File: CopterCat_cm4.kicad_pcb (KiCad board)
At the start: 4 copper layers, 99 parts, among them IC1 LY68L6400SLIT, J1 Micro_SD_Card, J2 Conn_01x08_Male, J3 Conn_01x08_Male, J4 Conn_01x08_Male, J5 XT30, U1 STM32H753IIKx, U10 ESP32-S2FH4, U11 W25Q128JVS, U12 U74AHC1G04G-AL5-R, U13 74LVC1G08GV, U14 NC7SZ02M5X, U2 ICM-20602, U3 BMP388, U4 FM25V02A-GTR, U5 BMM150, U6 Compute_Module_4_Connectors, U7 ICM-42605, U8 BMI088, U9 USB3300-EZK-TR, Y1 16MHz, Y2 32.768, Y3 24MHz, Y4 40MHz

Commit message: working
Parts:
- added J6: USB_C_Receptacle, Connector_USB:USB_C_Receptacle_XKB_U262-16XN-4BVC11, F.Cu at (170.2, 110.5)
- added U15: TPD4E02B04DQA, Package_SON:USON-10_2.5x1.0mm_P0.5mm, F.Cu at (147.3, 102.9)
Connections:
- U1 pad E15: STM_VBUS_SENSE -> PWR_IN2
- U9 pad 4: STM_VBUS_SENSE -> PWR_IN2

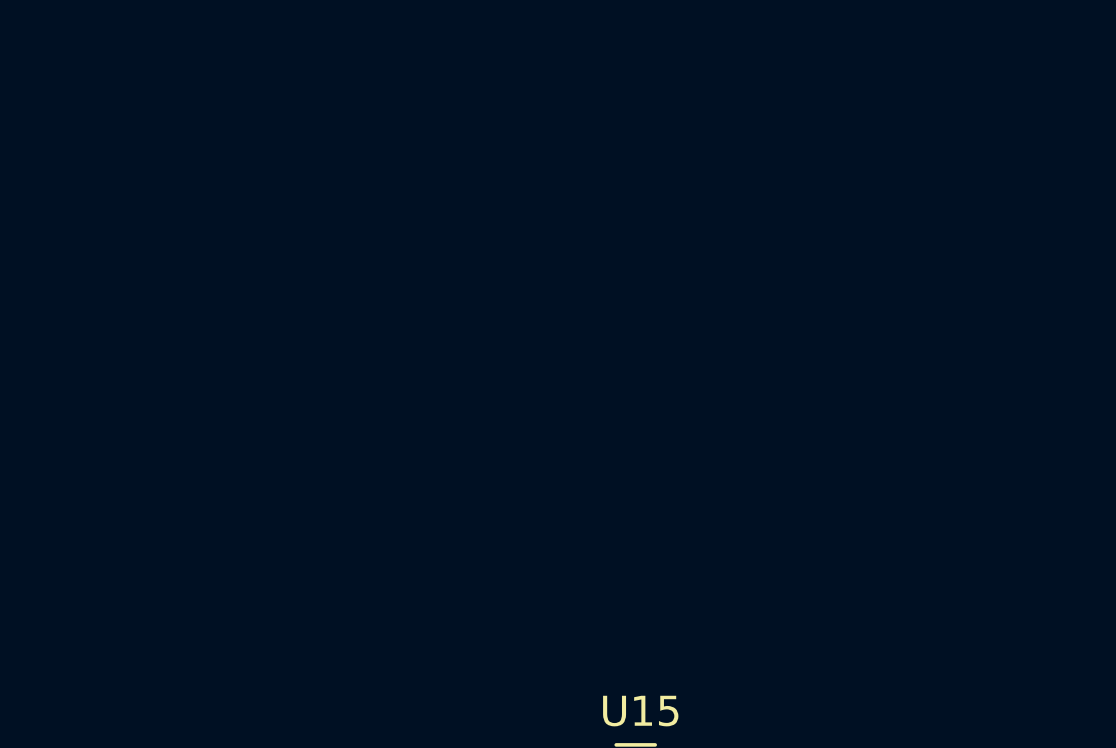
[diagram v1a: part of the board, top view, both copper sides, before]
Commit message: start migrating to kicad v6
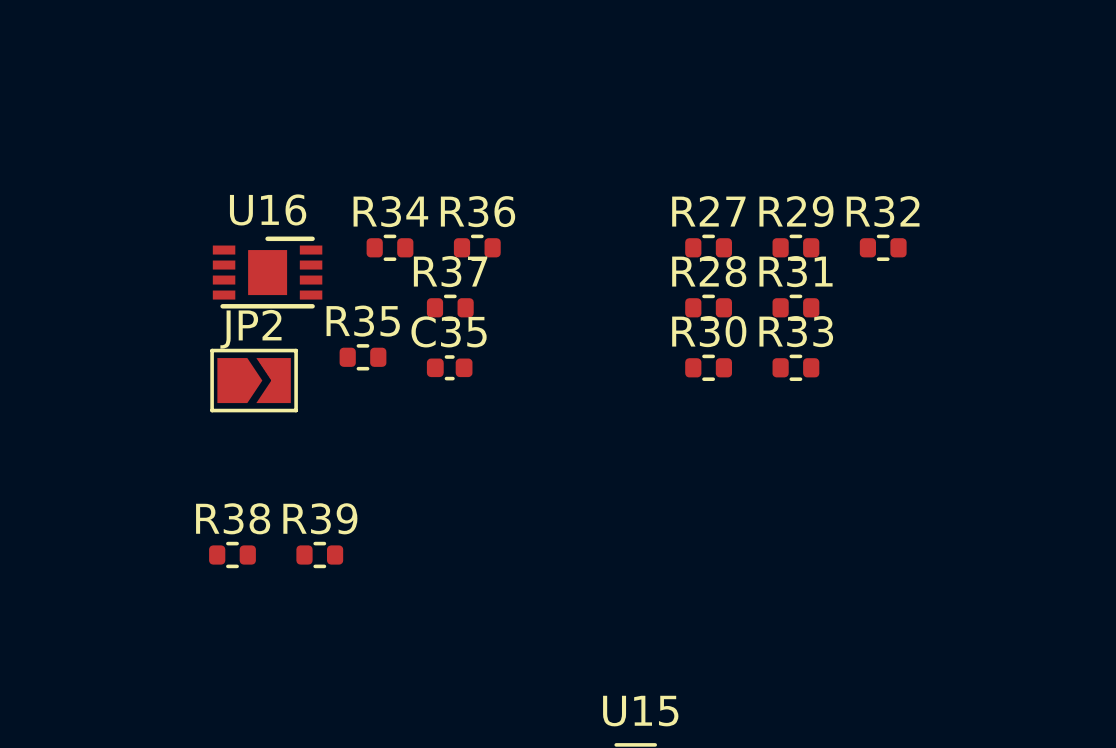
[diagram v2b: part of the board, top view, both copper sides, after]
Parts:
- added C35: 100nF, Capacitor_SMD:C_0402_1005Metric, F.Cu at (141.0, 88.9)
- added JP2: BOOT, Jumper:SolderJumper-2_P1.3mm_Open_TrianglePad1.0x1.5mm, F.Cu at (134.4, 89.3)
- added R27: DNP, Resistor_SMD:R_0402_1005Metric, F.Cu at (149.6, 84.9)
- added R28: DNP, Resistor_SMD:R_0402_1005Metric, F.Cu at (149.6, 86.9)
- added R29: DNP, Resistor_SMD:R_0402_1005Metric, F.Cu at (152.5, 84.9)
- added R30: DNP, Resistor_SMD:R_0402_1005Metric, F.Cu at (149.6, 88.9)
- added R31: 100R, Resistor_SMD:R_0402_1005Metric, F.Cu at (152.5, 86.9)
- added R32: 100R, Resistor_SMD:R_0402_1005Metric, F.Cu at (155.4, 84.9)
- added R33: 100R, Resistor_SMD:R_0402_1005Metric, F.Cu at (152.5, 88.9)
- added R34: 1K5, Resistor_SMD:R_0402_1005Metric, F.Cu at (139.0, 84.9)
- added R35: 100K, Resistor_SMD:R_0402_1005Metric, F.Cu at (138.1, 88.5)
- added R36: 100K, Resistor_SMD:R_0402_1005Metric, F.Cu at (141.9, 84.9)
- added R37: 100K, Resistor_SMD:R_0402_1005Metric, F.Cu at (141.0, 86.9)
- added R38: 5K1, Resistor_SMD:R_0402_1005Metric, F.Cu at (133.7, 95.1)
- added R39: 5K1, Resistor_SMD:R_0402_1005Metric, F.Cu at (136.6, 95.1)
- added U16: CAT24C256, Package_DFN_QFN:DFN-8-1EP_3x2mm_P0.5mm_EP1.3x1.5mm, F.Cu at (134.9, 85.7)
- JP1: value SolderJumper_2_Open -> BOOT
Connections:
- J6 pad A6: PWR_IN2 -> USB_FMU_D_P
- J6 pad A7: PWR_IN2 -> USB_FMU_D_N
- J6 pad B6: PWR_IN2 -> USB_FMU_D_P
- J6 pad B7: PWR_IN2 -> USB_FMU_D_N
- JP1 pad 1: Net-(JP1-Pad1) -> STM_3V3
- JP1 pad 2: STM_3V3 -> Net-(JP1-Pad2)
- R6 pad 1: Net-(JP1-Pad1) -> Net-(JP1-Pad2)
- U15 pad 4: Net-(U15-Pad4) -> USB_FMU_D_N
- U15 pad 5: Net-(U15-Pad5) -> USB_FMU_D_P
- U6 pad 93: Net-(U6-Pad93) -> RPI_NRPIBOOT

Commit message: доработка схемы + делаем красиво
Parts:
- removed J6: USB_C_Receptacle, Connector_USB:USB_C_Receptacle_XKB_U262-16XN-4BVC11
- removed the R20 at (106.6, 71.6)
- removed R30: DNP, Resistor_SMD:R_0402_1005Metric
- added ANT1: ANT016008LCS2442MA2, ANT016008LCS2442MA2:ANT_ANT016008LCS2442MA2, F.Cu at (209.9, 117.8)
- added C36: 100nF, Capacitor_SMD:C_0402_1005Metric, F.Cu at (113.9, 119.7)
- added C37: 100nF, Capacitor_SMD:C_0402_1005Metric, F.Cu at (117.0, 114.6)
- added L1: 3nH, Inductor_SMD:L_0402_1005Metric, F.Cu at (226.3, 103.6)
- added L2: 2nH, Inductor_SMD:L_0402_1005Metric, F.Cu at (216.5, 114.1)
- added Q1: Si7336ADP, Package_SO:PowerPAK_SO-8_Single, F.Cu at (95.0, 159.8)
- added Q2: Si7336ADP, Package_SO:PowerPAK_SO-8_Single, F.Cu at (95.0, 153.3)
- added R20: 4.7K, Resistor_SMD:R_0402_1005Metric, F.Cu at (112.9, 47.5)
- added R20: 4.7K, Resistor_SMD:R_0402_1005Metric, F.Cu at (56.9, 101.6)
- added R40: 10K, Resistor_SMD:R_0402_1005Metric, F.Cu at (105.7, 153.0)
- added R41: 10K, Resistor_SMD:R_0402_1005Metric, F.Cu at (113.9, 117.8)
- added U17: BMI088, BMI088:PQFN50P450X300X100-16N, F.Cu at (182.9, 47.3)
- C1, C3: value 100nF -> 2.2uF
- J5: value XT30 -> 5V; footprint Connector_AMASS:AMASS_XT30U-M_1x02_P5.0mm_Vertical -> Connector:power_pad
- JP2: value BOOT -> BR
- R1: value 0R -> 33R
- R10, R6, R9: value 10K -> 33R
- R11: value 10K -> DNP
- R2: value DNP -> 33R
- R22, R23, R24: value 33R -> 10K
- R25, R26: value 33R -> DNP
- R28: value DNP -> 10K
- R29: value DNP -> 4.7K
- R3, R8: value 10K -> 100R
- U8: value BMI088 -> CP2102N-Axx-xQFN28; footprint BMI088:PQFN50P450X300X100-16N -> Package_DFN_QFN:QFN-28-1EP_5x5mm_P0.5mm_EP3.35x3.35mm
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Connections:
- net ESP_NRST renamed /ESP32/ESP_NRST
- net ESP_SPI_3V3 renamed /ESP32/ESP_SPI_3V3
- net ESP_SPI_CIPO renamed /ESP32/ESP_SPI_CIPO
- net ESP_SPI_COPI renamed /ESP32/ESP_SPI_COPI
- net ESP_SPI_CS0 renamed /ESP32/ESP_SPI_CS0
- net ESP_SPI_CS1 renamed /ESP32/ESP_SPI_CS1
- net ESP_SPI_HLD renamed /ESP32/ESP_SPI_HLD
- net ESP_SPI_SCK renamed /ESP32/ESP_SPI_SCK
- net ESP_SPI_WP renamed /ESP32/ESP_SPI_WP
- net Net-(U6-Pad101) renamed /RPi_CM4/RPI_USB_ID
- net Net-(U6-Pad103) renamed /RPi_CM4/RPI_USB_N
- net Net-(U6-Pad105) renamed /RPi_CM4/RPI_USB_P
- net PWR_IN_5V_POWER renamed PWR_IN3
- net RPI_NRPIBOOT renamed /RPi_CM4/RPI_NRPIBOOT
- net RPI_SD_D2 renamed /RPi_CM4/RPI_SD_D2
- net STM_16MHZ_IN renamed /STM32/STM_16MHZ_IN
- net STM_16MHZ_OUT renamed /STM32/STM_16MHZ_OUT
- net STM_32KHZ_IN renamed /STM32/STM_32KHZ_IN
- net STM_32KHZ_OUT renamed /STM32/STM_32KHZ_OUT
- net STM_I2C2_DRDY1 renamed /STM32/STM_I2C4_DRDY1
- net STM_I2C2_SCL renamed /STM32/STM_I2C2_SCL
- net STM_I2C2_SDA renamed /STM32/STM_I2C2_SDA
- net STM_I2C3_SCL renamed /STM32/STM_I2C3_SCL
- net STM_I2C3_SDA renamed /STM32/STM_I2C3_SDA
- net STM_I2C4_DRDY1 renamed /Sensors/STM_I2C4_DRDY1
- net STM_NLED_BLUE renamed /STM32/STM_NLED_BLUE
- net STM_NLED_GREEN renamed /STM32/STM_NLED_GREEN
- net STM_NLED_RED renamed /STM32/STM_NLED_RED
- net STM_OTG_HS_ULPI_CK renamed /STM32/STM_OTG_HS_ULPI_CK
- net STM_OTG_HS_ULPI_D0 renamed /STM32/STM_OTG_HS_ULPI_D0
- net STM_OTG_HS_ULPI_D1 renamed /STM32/STM_OTG_HS_ULPI_D1
- net STM_OTG_HS_ULPI_D2 renamed /STM32/STM_OTG_HS_ULPI_D2
- net STM_OTG_HS_ULPI_D3 renamed /STM32/STM_OTG_HS_ULPI_D3
- net STM_OTG_HS_ULPI_D4 renamed /STM32/STM_OTG_HS_ULPI_D4
- net STM_OTG_HS_ULPI_D5 renamed /STM32/STM_OTG_HS_ULPI_D5
- net STM_OTG_HS_ULPI_D6 renamed /STM32/STM_OTG_HS_ULPI_D6
- net STM_OTG_HS_ULPI_D7 renamed /STM32/STM_OTG_HS_ULPI_D7
- net STM_OTG_HS_ULPI_DIR renamed /STM32/STM_OTG_HS_ULPI_DIR
- net STM_OTG_HS_ULPI_NXT renamed /STM32/STM_OTG_HS_ULPI_NXT
- net STM_OTG_HS_ULPI_STP renamed /STM32/STM_OTG_HS_ULPI_STP
- net STM_SP1_DRDY renamed /Sensors/STM_SPI1_DRDY1
- net STM_SPI1_DRDY1 renamed /STM32/STM_SPI1_DRDY1
- C1 pad 1: Net-(C1-Pad1) -> /STM32/STM_VCAP1
- C10 pad 1: STM_NRST -> /STM32/STM_NRST
- C2 pad 1: SENSORS_3V3 -> /STM32/STM_VCAP2
- C4 pad 1: SENSORS_3V3 -> Net-(C4-Pad1)
- CAM0 pad 11: Net-(CAM0-Pad11) -> unconnected-(CAM0-Pad11)
- CAM0 pad 12: Net-(CAM0-Pad12) -> unconnected-(CAM0-Pad12)
- CAM0 pad 14: Net-(CAM0-Pad14) -> unconnected-(CAM0-Pad14)
- CAM0 pad 15: Net-(CAM0-Pad15) -> unconnected-(CAM0-Pad15)
- CAM0 pad 18: Net-(CAM0-Pad18) -> unconnected-(CAM0-Pad18)
- CAM1 pad 18: Net-(CAM1-Pad18) -> unconnected-(CAM1-Pad18)
- J4 pad 1: STM_CH1 -> /Connectors/STM_CH1
- J4 pad 2: STM_CH2 -> /Connectors/STM_CH2
- J4 pad 3: STM_CH3 -> /Connectors/STM_CH3
- J4 pad 4: STM_CH4 -> /Connectors/STM_CH4
- J4 pad 5: STM_CH5 -> /Connectors/STM_CH5
- J4 pad 6: STM_CH6 -> /Connectors/STM_CH6
- J4 pad 7: STM_CH7 -> /Connectors/STM_CH7
- J4 pad 8: STM_CH8 -> /Connectors/STM_CH8
- J5 pad 2: /Power/VIN -> PWR_IN1
- R1 pad 1: Net-(R1-Pad1) -> /RPi_CM4/RPI_SD_D3
- R1 pad 2: GND -> Net-(J1-Pad2)
- R10 pad 1: SENSORS_3V3 -> Net-(J1-Pad8)
- R10 pad 2: STM_I2C4_SCL -> /RPi_CM4/RPI_SD_D1
- R11 pad 1: SENSORS_3V3 -> /STM32/STM_HW_VER_SENSE
- R11 pad 2: STM_I2C4_SDA -> /STM32/STM_HW_VER_REV_DRIVE
- R12 pad 1: STM_3V3 -> Net-(Q1-Pad4)
- R12 pad 2: STM_PDR_ON -> GND
- R13 pad 1: STM_3V3 -> SENSORS_3V3
- R13 pad 2: STM_NRST -> /STM32/STM_I2C4_SCL
- R2 pad 1: Net-(R1-Pad1) -> /RPi_CM4/RPI_SD_CMD
- R2 pad 2: SENSORS_3V3 -> Net-(J1-Pad3)
- R22 pad 1: RPI_SD_D3 -> SENSORS_3V3
- R22 pad 2: Net-(J1-Pad2) -> /STM32/STM_I2C4_SDA
- R23 pad 1: RPI_SD_CMD -> STM_3V3
- R23 pad 2: Net-(J1-Pad3) -> /STM32/STM_PDR_ON
- R24 pad 1: Net-(J1-Pad5) -> Net-(JP1-Pad2)
- R24 pad 2: RPI_SD_CLK -> /STM32/STM_BOOT0
- R25 pad 1: Net-(J1-Pad7) -> /STM32/STM_HW_REV_SENSE
- R25 pad 2: RPI_SD_D0 -> STM_3V3
- R26 pad 1: Net-(J1-Pad8) -> /STM32/STM_HW_VER_REV_DRIVE
- R26 pad 2: RPI_SD_D1 -> /STM32/STM_HW_REV_SENSE
- R27 pad 2: STM_HW_VER_SENSE -> /STM32/STM_HW_VER_SENSE
- R28 pad 1: STM_HW_VER_SENSE -> STM_3V3
- R28 pad 2: STM_HW_VER_REV_DRIVE -> /STM32/STM_NRST
- R29 pad 1: STM_HW_REV_SENSE -> RPI_I2C0_SCL
- R29 pad 2: STM_3V3 -> RPI_GPIO_VREF
- R3 pad 1: SENSORS_3V3 -> Net-(Q1-Pad4)
- R3 pad 2: Net-(R3-Pad2) -> PWR_EN2
- R6 pad 1: Net-(JP1-Pad2) -> Net-(J1-Pad5)
- R6 pad 2: STM_BOOT0 -> /RPi_CM4/RPI_SD_CLK
- R7 pad 2: STM_BOOT0 -> /STM32/STM_BOOT0
- R8 pad 1: GND -> Net-(Q2-Pad4)
- R8 pad 2: STM_VCAP1 -> PWR_EN3
- R9 pad 1: GND -> Net-(J1-Pad7)
- R9 pad 2: STM_VCAP2 -> /RPi_CM4/RPI_SD_D0
- U1 pad A5: STM_I2C1_SCL -> /STM32/STM_I2C1_SCL
- U1 pad B13: STM_SPI3_MISO -> /STM32/STM_SPI3_MISO
- U1 pad B14: STM_SPI3_SCK -> /STM32/STM_SPI3_SCK
- U1 pad B4: STM_I2C1_SDA -> /STM32/STM_I2C1_SDA
- U1 pad B9: STM_SPI1_SCK -> /STM32/STM_SPI1_SCK
- U1 pad C10: STM_SPI1_MISO -> /STM32/STM_SPI1_MISO
- U1 pad C13: STM_SPI2_MOSI -> /STM32/STM_SPI2_MOSI
- U1 pad C14: STM_SPI2_MISO -> /STM32/STM_SPI2_MISO
- U1 pad C2: STM_SPI3_DRDY2 -> /STM32/STM_SPI3_DRDY2
- U1 pad C3: STM_SPI3_DRDY1 -> /STM32/STM_SPI3_DRDY1
- U1 pad C6: STM_PDR_ON -> /STM32/STM_PDR_ON
- U1 pad D14: STM_SPI2_SCK -> /STM32/STM_SPI2_SCK
- U1 pad D15: STM_SPI2_DRDY2 -> /STM32/STM_SPI2_DRDY2
- U1 pad D2: STM_SPI3_CS2 -> /STM32/STM_SPI3_CS2
- U1 pad D3: STM_SPI1_CS1 -> /STM32/STM_SPI1_CS1
- U1 pad D4: STM_SPI3_CS1 -> /STM32/STM_SPI3_CS1
- U1 pad D6: STM_BOOT0 -> /STM32/STM_BOOT0
- U1 pad E14: STM_CH1 -> /STM32/STM_CH1
- U1 pad F13: STM_VCAP2 -> /STM32/STM_VCAP2
- U1 pad G4: STM_HW_VER_SENSE -> /STM32/STM_HW_VER_SENSE
- U1 pad H4: STM_HW_REV_SENSE -> /STM32/STM_HW_REV_SENSE
- U1 pad J1: STM_NRST -> /STM32/STM_NRST
- U1 pad J2: STM_I2C4_DRDY2 -> /STM32/STM_I2C4_DRDY2
- U1 pad J4: STM_SPI2_CS1 -> /STM32/STM_SPI2_CS1
- U1 pad K12: STM_CH2 -> /STM32/STM_CH2
- U1 pad L12: STM_CH3 -> /STM32/STM_CH3
- U1 pad L13: STM_CH4 -> /STM32/STM_CH4
- U1 pad M10: STM_VCAP1 -> /STM32/STM_VCAP1
- U1 pad M11: STM_CH7 -> /STM32/STM_CH7
- U1 pad M13: STM_CH8 -> /STM32/STM_CH8
- U1 pad M14: STM_CH6 -> /STM32/STM_CH6
- U1 pad M15: STM_CH5 -> /STM32/STM_CH5
- U1 pad M6: STM_SPI3_MOSI -> /STM32/STM_SPI3_MOSI
- U1 pad N7: STM_HW_VER_REV_DRIVE -> /STM32/STM_HW_VER_REV_DRIVE
- U1 pad P7: STM_I2C4_SDA -> /STM32/STM_I2C4_SDA
- U1 pad R3: STM_SPI1_MOSI -> /STM32/STM_SPI1_MOSI
- U1 pad R7: STM_I2C4_SCL -> /STM32/STM_I2C4_SCL
- U10 pad 10: Net-(U10-Pad10) -> unconnected-(U10-Pad10)
- U10 pad 11: Net-(U10-Pad11) -> unconnected-(U10-Pad11)
- U10 pad 12: Net-(U10-Pad12) -> unconnected-(U10-Pad12)
- U10 pad 13: Net-(U10-Pad13) -> unconnected-(U10-Pad13)
- U10 pad 14: Net-(U10-Pad14) -> unconnected-(U10-Pad14)
- U10 pad 15: Net-(U10-Pad15) -> unconnected-(U10-Pad15)
- U10 pad 16: Net-(U10-Pad16) -> unconnected-(U10-Pad16)
- U10 pad 17: Net-(U10-Pad17) -> unconnected-(U10-Pad17)
- U10 pad 18: Net-(U10-Pad18) -> unconnected-(U10-Pad18)
- U10 pad 19: Net-(U10-Pad19) -> unconnected-(U10-Pad19)
- U10 pad 21: Net-(U10-Pad21) -> unconnected-(U10-Pad21)
- U10 pad 22: Net-(U10-Pad22) -> unconnected-(U10-Pad22)
- U10 pad 23: Net-(U10-Pad23) -> unconnected-(U10-Pad23)
- U10 pad 24: Net-(U10-Pad24) -> unconnected-(U10-Pad24)
- U10 pad 25: Net-(U10-Pad25) -> unconnected-(U10-Pad25)
- U10 pad 26: Net-(U10-Pad26) -> unconnected-(U10-Pad26)
- U10 pad 28: Net-(U10-Pad28) -> unconnected-(U10-Pad28)
- U10 pad 37: Net-(U10-Pad37) -> unconnected-(U10-Pad37)
- U10 pad 38: Net-(U10-Pad38) -> unconnected-(U10-Pad38)
- U10 pad 39: Net-(U10-Pad39) -> unconnected-(U10-Pad39)
- U10 pad 40: Net-(U10-Pad40) -> unconnected-(U10-Pad40)
- U10 pad 41: Net-(U10-Pad41) -> unconnected-(U10-Pad41)
- U10 pad 42: Net-(U10-Pad42) -> unconnected-(U10-Pad42)
- U10 pad 43: Net-(U10-Pad43) -> unconnected-(U10-Pad43)
- U10 pad 44: Net-(U10-Pad44) -> unconnected-(U10-Pad44)
- U10 pad 46: Net-(U10-Pad46) -> unconnected-(U10-Pad46)
- U10 pad 47: Net-(U10-Pad47) -> unconnected-(U10-Pad47)
- U10 pad 48: Net-(U10-Pad48) -> unconnected-(U10-Pad48)
- U10 pad 49: Net-(U10-Pad49) -> unconnected-(U10-Pad49)
- U10 pad 5: Net-(U10-Pad5) -> unconnected-(U10-Pad5)
- U10 pad 50: Net-(U10-Pad50) -> unconnected-(U10-Pad50)
- U10 pad 55: Net-(U10-Pad55) -> unconnected-(U10-Pad55)
- U10 pad 6: Net-(U10-Pad6) -> unconnected-(U10-Pad6)
- U10 pad 7: Net-(U10-Pad7) -> unconnected-(U10-Pad7)
- U10 pad 8: Net-(U10-Pad8) -> unconnected-(U10-Pad8)
- U10 pad 9: Net-(U10-Pad9) -> unconnected-(U10-Pad9)
- U15 pad 10: Net-(U15-Pad10) -> unconnected-(U15-Pad10)
- U15 pad 2: Net-(U15-Pad2) -> unconnected-(U15-Pad2)
- U15 pad 6: Net-(U15-Pad6) -> unconnected-(U15-Pad6)
- U15 pad 7: Net-(U15-Pad7) -> unconnected-(U15-Pad7)
- U15 pad 9: Net-(U15-Pad9) -> unconnected-(U15-Pad9)
- U2 pad 14: Net-(C1-Pad1) -> Net-(C4-Pad1)
- U2 pad 2: STM_SPI1_SCK -> /Sensors/STM_SPI1_SCK
- U2 pad 3: STM_SPI1_MOSI -> /Sensors/STM_SPI1_MOSI
- U2 pad 4: STM_SPI1_MISO -> /Sensors/STM_SPI1_MISO
- U2 pad 5: STM_SPI1_CS1 -> /Sensors/STM_SPI1_CS1
- U2 pad 7: Net-(U2-Pad7) -> unconnected-(U2-Pad7)
- U3 pad 2: STM_I2C4_SCL -> /Sensors/STM_I2C4_SCL
- U3 pad 4: STM_I2C4_SDA -> /Sensors/STM_I2C4_SDA
- U3 pad 5: Net-(R1-Pad1) -> GND
- U3 pad 6: Net-(U3-Pad6) -> unconnected-(U3-Pad6)
- U5 pad A1: Net-(R3-Pad2) -> Net-(R41-Pad2)
- U5 pad A3: STM_I2C4_SCL -> /Sensors/STM_I2C4_SCL
- U5 pad B4: STM_I2C4_SDA -> /Sensors/STM_I2C4_SDA
- U5 pad D2: Net-(U5-PadD2) -> unconnected-(U5-PadD2)
- U5 pad D4: STM_I2C4_DRDY2 -> /Sensors/STM_I2C4_DRDY2
- U6 pad 10: Net-(U6-Pad10) -> unconnected-(U6-Pad10)
- U6 pad 100: Net-(U6-Pad100) -> unconnected-(U6-Pad100)
- U6 pad 102: Net-(U6-Pad102) -> unconnected-(U6-Pad102)
- U6 pad 104: Net-(U6-Pad104) -> unconnected-(U6-Pad104)
- U6 pad 106: Net-(U6-Pad106) -> unconnected-(U6-Pad106)
- U6 pad 109: Net-(U6-Pad109) -> unconnected-(U6-Pad109)
- U6 pad 11: Net-(U6-Pad11) -> unconnected-(U6-Pad11)
- U6 pad 110: Net-(U6-Pad110) -> unconnected-(U6-Pad110)
- U6 pad 111: Net-(U6-Pad111) -> unconnected-(U6-Pad111)
- U6 pad 112: Net-(U6-Pad112) -> unconnected-(U6-Pad112)
- U6 pad 116: Net-(U6-Pad116) -> unconnected-(U6-Pad116)
- U6 pad 118: Net-(U6-Pad118) -> unconnected-(U6-Pad118)
- U6 pad 12: Net-(U6-Pad12) -> unconnected-(U6-Pad12)
- U6 pad 122: Net-(U6-Pad122) -> unconnected-(U6-Pad122)
- U6 pad 124: Net-(U6-Pad124) -> unconnected-(U6-Pad124)
- U6 pad 143: Net-(U6-Pad143) -> unconnected-(U6-Pad143)
- U6 pad 145: Net-(U6-Pad145) -> unconnected-(U6-Pad145)
- U6 pad 146: Net-(U6-Pad146) -> unconnected-(U6-Pad146)
- U6 pad 147: Net-(U6-Pad147) -> unconnected-(U6-Pad147)
- U6 pad 148: Net-(U6-Pad148) -> unconnected-(U6-Pad148)
- U6 pad 149: Net-(U6-Pad149) -> unconnected-(U6-Pad149)
- U6 pad 15: Net-(U6-Pad15) -> unconnected-(U6-Pad15)
- U6 pad 151: Net-(U6-Pad151) -> unconnected-(U6-Pad151)
- U6 pad 152: Net-(U6-Pad152) -> unconnected-(U6-Pad152)
- U6 pad 153: Net-(U6-Pad153) -> unconnected-(U6-Pad153)
- U6 pad 154: Net-(U6-Pad154) -> unconnected-(U6-Pad154)
- U6 pad 157: Net-(U6-Pad157) -> unconnected-(U6-Pad157)
- U6 pad 158: Net-(U6-Pad158) -> unconnected-(U6-Pad158)
- U6 pad 159: Net-(U6-Pad159) -> unconnected-(U6-Pad159)
- U6 pad 16: Net-(U6-Pad16) -> unconnected-(U6-Pad16)
- U6 pad 160: Net-(U6-Pad160) -> unconnected-(U6-Pad160)
- U6 pad 163: Net-(U6-Pad163) -> unconnected-(U6-Pad163)
- U6 pad 164: Net-(U6-Pad164) -> unconnected-(U6-Pad164)
- U6 pad 165: Net-(U6-Pad165) -> unconnected-(U6-Pad165)
- U6 pad 166: Net-(U6-Pad166) -> unconnected-(U6-Pad166)
- U6 pad 169: Net-(U6-Pad169) -> unconnected-(U6-Pad169)
- U6 pad 17: Net-(U6-Pad17) -> unconnected-(U6-Pad17)
- U6 pad 170: Net-(U6-Pad170) -> unconnected-(U6-Pad170)
- U6 pad 171: Net-(U6-Pad171) -> unconnected-(U6-Pad171)
- U6 pad 172: Net-(U6-Pad172) -> unconnected-(U6-Pad172)
- U6 pad 175: Net-(U6-Pad175) -> unconnected-(U6-Pad175)
- U6 pad 176: Net-(U6-Pad176) -> unconnected-(U6-Pad176)
- U6 pad 177: Net-(U6-Pad177) -> unconnected-(U6-Pad177)
- U6 pad 178: Net-(U6-Pad178) -> unconnected-(U6-Pad178)
- U6 pad 18: Net-(U6-Pad18) -> unconnected-(U6-Pad18)
- U6 pad 181: Net-(U6-Pad181) -> unconnected-(U6-Pad181)
- U6 pad 182: Net-(U6-Pad182) -> unconnected-(U6-Pad182)
- U6 pad 183: Net-(U6-Pad183) -> unconnected-(U6-Pad183)
- U6 pad 184: Net-(U6-Pad184) -> unconnected-(U6-Pad184)
- U6 pad 187: Net-(U6-Pad187) -> unconnected-(U6-Pad187)
- U6 pad 188: Net-(U6-Pad188) -> unconnected-(U6-Pad188)
- U6 pad 189: Net-(U6-Pad189) -> unconnected-(U6-Pad189)
- U6 pad 19: Net-(U6-Pad19) -> unconnected-(U6-Pad19)
- U6 pad 190: Net-(U6-Pad190) -> unconnected-(U6-Pad190)
- U6 pad 193: Net-(U6-Pad193) -> unconnected-(U6-Pad193)
- U6 pad 194: Net-(U6-Pad194) -> unconnected-(U6-Pad194)
- U6 pad 195: Net-(U6-Pad195) -> unconnected-(U6-Pad195)
- U6 pad 196: Net-(U6-Pad196) -> unconnected-(U6-Pad196)
- U6 pad 199: Net-(U6-Pad199) -> unconnected-(U6-Pad199)
- U6 pad 20: Net-(U6-Pad20) -> unconnected-(U6-Pad20)
- U6 pad 200: Net-(U6-Pad200) -> unconnected-(U6-Pad200)
- U6 pad 21: Net-(U6-Pad21) -> unconnected-(U6-Pad21)
- U6 pad 24: Net-(U6-Pad24) -> unconnected-(U6-Pad24)
- U6 pad 26: Net-(U6-Pad26) -> unconnected-(U6-Pad26)
- U6 pad 27: Net-(U6-Pad27) -> unconnected-(U6-Pad27)
- U6 pad 28: Net-(U6-Pad28) -> unconnected-(U6-Pad28)
- U6 pad 29: Net-(U6-Pad29) -> unconnected-(U6-Pad29)
- U6 pad 3: Net-(U6-Pad3) -> unconnected-(U6-Pad3)
- U6 pad 30: Net-(U6-Pad30) -> unconnected-(U6-Pad30)
- U6 pad 31: Net-(U6-Pad31) -> unconnected-(U6-Pad31)
- U6 pad 34: Net-(U6-Pad34) -> unconnected-(U6-Pad34)
- U6 pad 37: Net-(U6-Pad37) -> unconnected-(U6-Pad37)
- U6 pad 38: Net-(U6-Pad38) -> unconnected-(U6-Pad38)
- U6 pad 39: Net-(U6-Pad39) -> unconnected-(U6-Pad39)
- U6 pad 4: Net-(U6-Pad4) -> unconnected-(U6-Pad4)
- U6 pad 40: Net-(U6-Pad40) -> unconnected-(U6-Pad40)
- U6 pad 41: Net-(U6-Pad41) -> unconnected-(U6-Pad41)
- U6 pad 44: Net-(U6-Pad44) -> unconnected-(U6-Pad44)
- U6 pad 45: Net-(U6-Pad45) -> unconnected-(U6-Pad45)
- U6 pad 46: Net-(U6-Pad46) -> unconnected-(U6-Pad46)
- U6 pad 47: Net-(U6-Pad47) -> unconnected-(U6-Pad47)
- U6 pad 48: Net-(U6-Pad48) -> unconnected-(U6-Pad48)
- U6 pad 49: Net-(U6-Pad49) -> unconnected-(U6-Pad49)
- U6 pad 5: Net-(U6-Pad5) -> unconnected-(U6-Pad5)
- U6 pad 50: Net-(U6-Pad50) -> unconnected-(U6-Pad50)
- U6 pad 51: Net-(U6-Pad51) -> unconnected-(U6-Pad51)
- U6 pad 54: Net-(U6-Pad54) -> unconnected-(U6-Pad54)
- U6 pad 55: Net-(U6-Pad55) -> unconnected-(U6-Pad55)
- U6 pad 57: RPI_SD_CLK -> /RPi_CM4/RPI_SD_CLK
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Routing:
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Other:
- copper layers 4 -> 2
- net class Default removed
- net class Signal removed

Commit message: плата практически готова
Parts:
- removed C29: 4.7uF, Capacitor_SMD:C_0402_1005Metric
- removed F1: Fuse, Fuse:Fuse_0603_1608Metric
- removed J1: Micro_SD_Card, Connector_Card:microSD_HC_Wuerth_693072010801
- removed the R20 at (112.9, 47.5)
- removed the R20 at (56.9, 101.6)
- added C38: 10uF, Capacitor_Tantalum_SMD:CP_EIA-3216-18_Kemet-A, F.Cu at (236.7, 86.2)
- added C39: 10uF, Capacitor_Tantalum_SMD:CP_EIA-3216-18_Kemet-A, B.Cu at (236.1, 94.5)
- added C40: 10uF, Capacitor_Tantalum_SMD:CP_EIA-3216-18_Kemet-A, F.Cu at (229.8, 96.8)
- added C41: 10uF, Capacitor_Tantalum_SMD:CP_EIA-3216-18_Kemet-A, F.Cu at (242.7, 127.7)
- added C42: 100nF, Capacitor_SMD:C_0402_1005Metric, F.Cu at (225.1, 96.5)
- added C43: 100nF, Capacitor_SMD:C_0402_1005Metric, F.Cu at (227.0, 96.5)
- added C44: 100nF, Capacitor_SMD:C_0402_1005Metric, F.Cu at (226.1, 96.5)
- added D1: LED_RBAG, LED_SMD:LED_Cree-PLCC4_2x2mm_CW, B.Cu at (238.2, 108.2)
- added D5: 1N5819WS, Diode_SMD:D_SOD-323, F.Cu at (224.9, 124.8)
- added D7: 1N5819WS, Diode_SMD:D_SOD-323, B.Cu at (214.8, 100.0)
- added J6: USB_C_Receptacle_USB2.0, Connector_USB:USB_C_Receptacle_HRO_TYPE-C-31-M-12, B.Cu at (235.8, 133.2)
- added J7: USB_SWITCH, Connector_PinHeader_2.54mm:PinHeader_1x02_P2.54mm_Vertical, B.Cu at (215.2, 103.2)
- added Q3: MUN5211DW1, Package_TO_SOT_SMD:SOT-363_SC-70-6, F.Cu at (216.0, 94.6)
- added Q4: AO3400A, Package_TO_SOT_SMD:SOT-23, F.Cu at (237.4, 133.0)
- added Q5: AO3400A, Package_TO_SOT_SMD:SOT-23, F.Cu at (234.0, 133.0)
- added Q6: 2N7002K, Package_TO_SOT_SMD:SOT-23, F.Cu at (238.4, 117.5)
- added Q7: FDN340P, Package_TO_SOT_SMD:SOT-23, F.Cu at (233.7, 118.8)
- added Q8: DMP3013SFV, Package_SON:Diodes_PowerDI3333-8, F.Cu at (244.1, 91.8)
- added R20: 4.7K, Resistor_SMD:R_0402_1005Metric, F.Cu at (241.5, 101.3)
- added R20: 4.7K, Resistor_SMD:R_0402_1005Metric, F.Cu at (240.7, 108.1)
- added R42: 1K, Resistor_SMD:R_0402_1005Metric, B.Cu at (220.3, 98.8)
- added R43: 10K, Resistor_SMD:R_0402_1005Metric, F.Cu at (236.2, 119.2)
- added R44: 10K, Resistor_SMD:R_0402_1005Metric, F.Cu at (236.2, 117.2)
- added R45: 10K, Resistor_SMD:R_0402_1005Metric, B.Cu at (220.0, 114.8)
- added R46: 10K, Resistor_SMD:R_0402_1005Metric, B.Cu at (220.0, 112.9)
- added R47: 220R, Resistor_SMD:R_0402_1005Metric, F.Cu at (246.5, 92.8)
- added R48: 100K, Resistor_SMD:R_0402_1005Metric, F.Cu at (224.7, 107.0)
- added R49: 100K, Resistor_SMD:R_0402_1005Metric, F.Cu at (228.1, 107.4)
- added R50: 220R, Resistor_SMD:R_0402_1005Metric, F.Cu at (239.1, 127.1)
- added R51: 12K, Resistor_SMD:R_0402_1005Metric, F.Cu at (229.0, 100.1)
- added R52: 100K, Resistor_SMD:R_0402_1005Metric, F.Cu at (229.5, 105.4)
- added R53: 100K, Resistor_SMD:R_0402_1005Metric, F.Cu at (226.6, 107.0)
- added R54: 10K, Resistor_SMD:R_0402_1005Metric, F.Cu at (231.5, 132.3)
- added R55: 10K, Resistor_SMD:R_0402_1005Metric, F.Cu at (238.6, 129.6)
- added R56: 10K, Resistor_SMD:R_0402_1005Metric, F.Cu at (246.5, 90.2)
- added U18: FSUSB42MUX, Package_DFN_QFN:UQFN-10_1.4x1.8mm_P0.4mm, B.Cu at (228.5, 104.5)
- added U19: USB2514B_Bi, Package_DFN_QFN:QFN-36-1EP_6x6mm_P0.5mm_EP3.7x3.7mm, F.Cu at (224.9, 102.9)
- added U21: 47579-0001, 47579-0001:POS-8, B.Cu at (234.9, 101.8)
- ANT1, C1, C13, C14, C15, C16, C2, C3, C32, C33, C34, C36, C37, C4, C5, CAM0, F2, F3, GPS1, I2C1, J2, J3, J4, J5, JP2, L1, L2, LASER1, POWER1, R1, R10, R2, R21, R31, R32, R33, R34, R4, R41, R5, R6, R9, RC1, TELEM1, TELEM2, U10, U11, U17, U2, U4, U5, U7: moved to B.Cu
- C11, C8: value 10pF -> 15pF
- C19: value 12pF -> 100nF; moved to B.Cu
- C20: value 12pF -> 15pF
- C21: value 100nF -> 15pF
- C22, C23: value 100nF -> 2.2uF
- C24, C25: value 100nF -> 22uF
- C26: value 4.7uF -> 22uF; moved to B.Cu
- C27: value 4.7uF -> 22uF
- C28: value 4.7uF -> 10uF; footprint Capacitor_SMD:C_0402_1005Metric -> Capacitor_Tantalum_SMD:CP_EIA-3216-18_Kemet-A; moved to B.Cu
- C30, C31: value 18pF -> 15pF; moved to B.Cu
- Q1: value Si7336ADP -> MMDT3906; footprint Package_SO:PowerPAK_SO-8_Single -> Package_TO_SOT_SMD:SOT-363_SC-70-6; moved to B.Cu
- Q2: value Si7336ADP -> DMP3013SFV; footprint Package_SO:PowerPAK_SO-8_Single -> Package_SON:Diodes_PowerDI3333-8; moved to B.Cu
- R12: value 10K -> 1M; moved to B.Cu
- R13, R22: value 10K -> 4K7; moved to B.Cu
- R14: value 10K -> 1K; moved to B.Cu
- R19, R29: value 4.7K -> 4K7
- R3: value 100R -> 4K7; moved to B.Cu
- R40: value 10K -> 100K; moved to B.Cu
- R8: value 100R -> 220R
- STM_DEBUG1: footprint Connector:Tag-Connect_TC2030-IDC-NL_2x03_P1.27mm_Vertical -> Connector:debug_port
- U12: value U74AHC1G04G-AL5-R -> AMS1117-3.3; footprint Package_TO_SOT_SMD:SOT-353_SC-70-5 -> Package_TO_SOT_SMD:SOT-223-3_TabPin2
- U13: value 74LVC1G08GV -> 74AHC1G04; footprint Package_TO_SOT_SMD:SOT-23-5 -> Package_TO_SOT_SMD:SOT-353_SC-70-5
- U14: value NC7SZ02M5X -> FSUSB42MUX; footprint Package_TO_SOT_SMD:SOT-23-5 -> Package_DFN_QFN:UQFN-10_1.4x1.8mm_P0.4mm; moved to B.Cu
- U8: value CP2102N-Axx-xQFN28 -> CP2104; footprint Package_DFN_QFN:QFN-28-1EP_5x5mm_P0.5mm_EP3.35x3.35mm -> Package_DFN_QFN:QFN-24-1EP_4x4mm_P0.5mm_EP2.6x2.6mm
- U9: value USB3300-EZK-TR -> AMS1117-3.3; footprint Package_DFN_QFN:QFN-32-1EP_5x5mm_P0.5mm_EP3.45x3.45mm -> Package_TO_SOT_SMD:SOT-223-3_TabPin2
- Y1, Y3: footprint Crystal:Crystal_SMD_2520-4Pin_2.5x2.0mm -> Crystal:Crystal_SMD_2016-4Pin_2.0x1.6mm
- Y2: footprint Crystal:Crystal_SMD_3215-2Pin_3.2x1.5mm -> Crystal:Crystal_SMD_MicroCrystal_CM9V-T1A-2Pin_1.6x1.0mm
- Y4: footprint Crystal:Crystal_SMD_2520-4Pin_2.5x2.0mm -> Crystal:Crystal_SMD_2016-4Pin_2.0x1.6mm; moved to B.Cu
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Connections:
- net /STM32/STM_I2C2_SCL renamed /STM32/STM_I2C2.SCL
- net /STM32/STM_I2C2_SDA renamed /STM32/STM_I2C2.SDA
- net /STM32/STM_I2C3_SCL renamed /STM32/STM_I2C3.SCL
- net /STM32/STM_I2C3_SDA renamed /STM32/STM_I2C3.SDA
- net PWR_IN3 renamed /Connectors/PWR_IN_JST
- net RPI_CAM0_C_N renamed /Connectors/RPI_CAM0.C_N
- net RPI_CAM0_C_P renamed /Connectors/RPI_CAM0.C_P
- net RPI_CAM0_D0_N renamed /Connectors/RPI_CAM0.D_N0
- net RPI_CAM0_D0_P renamed /Connectors/RPI_CAM0.D_P0
- net RPI_CAM0_D1_N renamed /Connectors/RPI_CAM0.D_N1
- net RPI_CAM0_D1_P renamed /Connectors/RPI_CAM0.D_P1
- net RPI_CAM1_C_N renamed /Connectors/RPI_CAM1.C_N
- net RPI_CAM1_C_P renamed /Connectors/RPI_CAM1.C_P
- net RPI_CAM1_D0_N renamed /Connectors/RPI_CAM1.D_N0
- net RPI_CAM1_D0_P renamed /Connectors/RPI_CAM1.D_P0
- net RPI_CAM1_D1_N renamed /Connectors/RPI_CAM1.D_N1
- net RPI_CAM1_D1_P renamed /Connectors/RPI_CAM1.D_P1
- net RPI_CAM1_D2_N renamed /Connectors/RPI_CAM1.D_N2
- net RPI_CAM1_D2_P renamed /Connectors/RPI_CAM1.D_P2
- net RPI_CAM1_D3_N renamed /Connectors/RPI_CAM1.D_N3
- net RPI_CAM1_D3_P renamed /Connectors/RPI_CAM1.D_P3
- net RPI_CAM_GPIO renamed /Connectors/RPI_CAM_GPIO
- net RPI_GPIO21 renamed /Connectors/RPI_GPIO21
- net RPI_GPIO_VREF renamed /Connectors/RPI_OUT_3V3
- net RPI_LASER_I2C_SCL renamed /Connectors/RPI_LASER_I2C.SCL
- net RPI_LASER_I2C_SDA renamed /Connectors/RPI_LASER_I2C.SDA
- net SENSORS_3V3 renamed /STM32/SENSORS_3V3
- net STM_ADC3_3V3 renamed /Connectors/STM_ADC.3V3
- net STM_ADC3_6V6 renamed /Connectors/STM_ADC.6V6
- net STM_PPM_INPUT renamed /Connectors/STM_RC.PPM
- net STM_SPI4_CS1 renamed /STM32/STM_SPI4.CS1
- net STM_SPI4_MISO renamed /STM32/STM_SPI4.MISO
- net STM_SPI4_MOSI renamed /STM32/STM_SPI4.MOSI
- net STM_SPI4_SCK renamed /STM32/STM_SPI4.SCK
- net STM_SPI5_CS1 renamed /STM32/STM_SPI5_CS1
- net STM_SPI5_MISO renamed /STM32/STM_SPI5_MISO
- net STM_SPI5_MOSI renamed /STM32/STM_SPI5_MOSI
- net STM_SPI5_SCK renamed /STM32/STM_SPI5_SCK
- net STM_SPI6_CS1 renamed /STM32/STM_SPI6.CS1
- net STM_SPI6_CS2 renamed /STM32/STM_SPI6.CS2
- net STM_SPI6_DRDY1 renamed /STM32/STM_SPI6.DRDY1
- net STM_SPI6_DRDY2 renamed /STM32/STM_SPI6.DRDY2
- net STM_SPI6_MISO renamed /STM32/STM_SPI6.MISO
- net STM_SPI6_MOSI renamed /STM32/STM_SPI6.MOSI
- net STM_SPI6_NRESET renamed /STM32/STM_SPI6.NRESET
- net STM_SPI6_SCK renamed /STM32/STM_SPI6.SCK
- net STM_UART4_RX renamed /STM32/STM_UART4.RX
- net STM_UART4_TX renamed /STM32/STM_UART4.TX
- net STM_UART5_CTS renamed /Connectors/STM_UART5.CTS
- net STM_UART5_RTS renamed /Connectors/STM_UART5.RTS
- net STM_UART5_RX renamed /Connectors/STM_UART5.RX
- net STM_UART5_TX renamed /Connectors/STM_UART5.TX
- net STM_UART7_CTS renamed /Connectors/STM_UART7.CTS
- net STM_UART7_RTS renamed /Connectors/STM_UART7.RTS
- net STM_UART7_RX renamed /Connectors/STM_UART7.RX
- net STM_UART7_TX renamed /Connectors/STM_UART7.TX
- net STM_UART8_RX renamed /STM32/STM_UART8.RX
- net STM_UART8_TX renamed /STM32/STM_UART8.TX
- net STM_USART1_RX renamed /Connectors/STM_USART1.RX
- net STM_USART1_TX renamed /Connectors/STM_USART1.TX
- net STM_USART2_CTS renamed /ESP32/ESP_UART1.CTS
- net STM_USART2_RTS renamed /ESP32/ESP_UART1.RTS
- net STM_USART3_RX renamed /Connectors/STM_DEBUG.RX
- net STM_USART3_TX renamed /Connectors/STM_DEBUG.TX
- net STM_USART6_RX renamed /Connectors/STM_RC.RX
- net STM_USART6_TX renamed /STM32/STM_USART6_TX
- C19 pad 1: GND -> /ESP32/ESP_NRST
- C19 pad 2: Net-(C19-Pad2) -> GND
- C20 pad 1: Net-(C20-Pad1) -> GND
- C20 pad 2: GND -> Net-(C20-Pad2)
- C21 pad 1: GND -> Net-(C21-Pad1)
- C21 pad 2: Net-(C21-Pad2) -> GND
- C22 pad 1: STM_3V3 -> GND
- C22 pad 2: GND -> /ESP32/ESP_3V3
- C23 pad 1: STM_3V3 -> /ESP32/ESP_3V3
- C24 pad 1: STM_3V3 -> GND
- C24 pad 2: GND -> VCC
- C25 pad 1: STM_3V3 -> /Power/5V_GROUP2
- C26 pad 1: GND -> /Power/3V3_GROUP1
- C26 pad 2: STM_1V8 -> GND
- C27 pad 1: GND -> /ESP32/ESP_3V3
- C27 pad 2: STM_1V8 -> GND
- C28 pad 1: GND -> /Power/3V3_GROUP1
- C28 pad 2: STM_1V8 -> GND
- C32 pad 1: ESP_3V3 -> /ESP32/ESP_3V3
- C33 pad 1: ESP_3V3 -> /ESP32/ESP_3V3
- C34 pad 1: ESP_3V3 -> /ESP32/ESP_3V3
- CAM0 pad 20: RPI_I2C1_SCL -> /Connectors/RPI_I2C1.SCL
- CAM0 pad 21: RPI_I2C1_SDA -> /Connectors/RPI_I2C1.SDA
- CAM1 pad 20: RPI_I2C0_SCL -> /Connectors/RPI_I2C0.SCL
- CAM1 pad 21: RPI_I2C0_SDA -> /Connectors/RPI_I2C0.SDA
- F2 pad 1: ESP_3V3 -> /ESP32/ESP_3V3
- F3 pad 1: ESP_3V3 -> /ESP32/ESP_3V3
- GPS1 pad 2: STM_I2C1_SDA -> /Connectors/STM_I2C1.SDA
- GPS1 pad 3: STM_I2C1_SCL -> /Connectors/STM_I2C1.SCL
- GPS1 pad 6: PERIPH_V5 -> VCC
- I2C1 pad 2: STM_I2C1_SDA -> /Connectors/STM_I2C1.SDA
- I2C1 pad 3: STM_I2C1_SCL -> /Connectors/STM_I2C1.SCL
- I2C1 pad 4: PERIPH_V5 -> VCC
- J4 pad 1: /Connectors/STM_CH1 -> /Connectors/STM_ESC.CH1
- J4 pad 2: /Connectors/STM_CH2 -> /Connectors/STM_ESC.CH2
- J4 pad 3: /Connectors/STM_CH3 -> /Connectors/STM_ESC.CH3
- J4 pad 4: /Connectors/STM_CH4 -> /Connectors/STM_ESC.CH4
- J4 pad 5: /Connectors/STM_CH5 -> /Connectors/STM_ESC.CH5
- J4 pad 6: /Connectors/STM_CH6 -> /Connectors/STM_ESC.CH6
- J4 pad 7: /Connectors/STM_CH7 -> /Connectors/STM_ESC.CH7
- J4 pad 8: /Connectors/STM_CH8 -> /Connectors/STM_ESC.CH8
- J5 pad 2: PWR_IN1 -> /Connectors/LED_V5
- JP1 pad 1: STM_3V3 -> /Power/3V3_GROUP1
- LED1 pad 1: LED_V5 -> /Connectors/LED_V5
- Q1 pad 1: GND -> /Connectors/LED_V5
- Q1 pad 2: GND -> Net-(Q1-Pad2)
- Q1 pad 3: GND -> Net-(Q1-Pad3)
- Q1 pad 4: Net-(Q1-Pad4) -> VCC
- Q1 pad 5: unconnected-(Q1-Pad5) -> Net-(Q1-Pad2)
- Q2 pad 1: GND -> VCC
- Q2 pad 2: GND -> VCC
- Q2 pad 3: GND -> VCC
- Q2 pad 4: Net-(Q2-Pad4) -> Net-(Q1-Pad3)
- Q2 pad 5: unconnected-(Q2-Pad5) -> /Connectors/LED_V5
- R12 pad 1: Net-(Q1-Pad4) -> Net-(Q1-Pad2)
- R13 pad 2: /STM32/STM_I2C4_SCL -> /STM32/STM_I2C4.SCL
- R14 pad 1: GND -> Net-(R14-Pad1)
- R14 pad 2: Net-(R14-Pad2) -> /ESP32/ESP_UART0_TX
- R15 pad 1: ESP_3V3 -> /ESP32/ESP_3V3
- R16 pad 1: ESP_3V3 -> /ESP32/ESP_3V3
- R17 pad 2: ESP_3V3 -> /ESP32/ESP_3V3
- R18 pad 2: ESP_3V3 -> /ESP32/ESP_3V3
- R19 pad 1: RPI_I2C1_SCL -> /Connectors/RPI_I2C0.SDA
- R22 pad 2: /STM32/STM_I2C4_SDA -> /STM32/STM_I2C4.SDA
- R23 pad 1: STM_3V3 -> /Power/3V3_GROUP1
- R25 pad 2: STM_3V3 -> /Power/3V3_GROUP1
- R27 pad 1: STM_3V3 -> /Power/3V3_GROUP1
- R28 pad 1: STM_3V3 -> /Power/3V3_GROUP1
- R29 pad 1: RPI_I2C0_SCL -> /Connectors/RPI_I2C1.SDA
- R3 pad 1: Net-(Q1-Pad4) -> /RPi_CM4/RPI_USB.ID
- R3 pad 2: PWR_EN2 -> GND
- R32 pad 1: /STM32/STM_NLED_GREEN -> Net-(D1-Pad4)
- R32 pad 2: Net-(D2-Pad1) -> /STM32/STM_NLED_GREEN
- R4 pad 1: STM_3V3 -> /Power/3V3_GROUP1
- R40 pad 1: Net-(Q2-Pad4) -> Net-(Q1-Pad3)
- R5 pad 1: STM_3V3 -> /Power/3V3_GROUP1
- R8 pad 1: Net-(Q2-Pad4) -> Net-(Q5-Pad1)
- R8 pad 2: PWR_EN3 -> /RPi_CM4/RPI_USB.ID
- RC1 pad 2: STM_VDD_3V3_SPEKTRUM_POWER_EN -> /Connectors/STM_RC.PWR
- RC1 pad 5: PERIPH_V5 -> VCC
- STM_DEBUG1 pad 4: STM_SWDIO -> /Connectors/STM_DEBUG.SWCLK
- STM_DEBUG1 pad 5: STM_SWCLK -> /Connectors/STM_DEBUG.SWDIO
- STM_DEBUG1 pad 6: STM_3V3 -> /Connectors/STM_DEBUG.3V3
- TELEM1 pad 4: PERIPH_V5 -> VCC
- TELEM2 pad 4: PERIPH_V5 -> VCC
- U1 pad A14: STM_SWCLK -> /Connectors/STM_DEBUG.SWCLK
- U1 pad A15: STM_SWDIO -> /Connectors/STM_DEBUG.SWDIO
- U1 pad A5: /STM32/STM_I2C1_SCL -> /Connectors/STM_I2C1.SCL
- U1 pad B11: STM_USART2_RX -> /ESP32/ESP_UART1.RX
- U1 pad B13: /STM32/STM_SPI3_MISO -> /STM32/STM_SPI3.MISO
- U1 pad B14: /STM32/STM_SPI3_SCK -> /STM32/STM_SPI3.SCK
- U1 pad B15: STM_USB_D_P -> /STM32/STM_USB.DP
- U1 pad B4: /STM32/STM_I2C1_SDA -> /Connectors/STM_I2C1.SDA
- U1 pad B8: STM_VDD_3V3_SENSORS_EN -> /STM32/STM_VDD_3V3_SENSORS_EN
- U1 pad B9: /STM32/STM_SPI1_SCK -> /STM32/STM_SPI1.SCK
- U1 pad C1: STM_VBAT -> /Power/3V3_GROUP1
- U1 pad C10: /STM32/STM_SPI1_MISO -> /STM32/STM_SPI1.MISO
- U1 pad C11: STM_USART2_TX -> /ESP32/ESP_UART1.TX
- U1 pad C13: /STM32/STM_SPI2_MOSI -> /STM32/STM_SPI2.MOSI
- U1 pad C14: /STM32/STM_SPI2_MISO -> /STM32/STM_SPI2.MISO
- U1 pad C15: STM_USB_D_N -> /STM32/STM_USB.DN
- U1 pad C2: /STM32/STM_SPI3_DRDY2 -> /STM32/STM_SPI3.DRDY2
- U1 pad C3: /STM32/STM_SPI3_DRDY1 -> /STM32/STM_SPI3.DRDY1
- U1 pad C5: STM_3V3 -> /Power/3V3_GROUP1
- U1 pad C7: STM_3V3 -> /Power/3V3_GROUP1
- U1 pad C8: STM_3V3 -> /Power/3V3_GROUP1
- U1 pad C9: STM_3V3 -> /Power/3V3_GROUP1
- U1 pad D14: /STM32/STM_SPI2_SCK -> /STM32/STM_SPI2.SCK
- U1 pad D15: /STM32/STM_SPI2_DRDY2 -> /STM32/STM_SPI2.DRDY2
- U1 pad D2: /STM32/STM_SPI3_CS2 -> /STM32/STM_SPI3.CS2
- U1 pad D3: /STM32/STM_SPI1_CS1 -> /STM32/STM_SPI1.CS1
- U1 pad D4: /STM32/STM_SPI3_CS1 -> /STM32/STM_SPI3.CS1
- U1 pad E14: /STM32/STM_CH1 -> /Connectors/STM_ESC.CH1
- U1 pad E15: PWR_IN2 -> /STM32/STM_USB.VBUS
- U1 pad F3: STM_3V3 -> /Power/3V3_GROUP1
- U1 pad F4: STM_VDD_3V3_SPEKTRUM_POWER_EN -> /STM32/STM_VDD_3V3_SPEKTRUM_POWER_EN
- U1 pad G10: STM_3V3 -> /Power/3V3_GROUP1
- U1 pad G13: STM_3V3 -> /Power/3V3_GROUP1
- U1 pad G3: STM_3V3 -> /Power/3V3_GROUP1
- U1 pad H13: STM_3V3 -> /Power/3V3_GROUP1
- U1 pad H2: /STM32/STM_SPI1_DRDY1 -> /STM32/STM_SPI1.DRDY1
- U1 pad J12: STM_3V3 -> /Power/3V3_GROUP1
- U1 pad J13: STM_3V3 -> /Power/3V3_GROUP1
- U1 pad J2: /STM32/STM_I2C4_DRDY2 -> /STM32/STM_I2C4.DRDY2
- U1 pad J4: /STM32/STM_SPI2_CS1 -> /STM32/STM_SPI2.CS1
- U1 pad K12: /STM32/STM_CH2 -> /Connectors/STM_ESC.CH2
- U1 pad K13: /STM32/STM_I2C4_DRDY1 -> /STM32/STM_I2C4.DRDY1
- U1 pad K4: STM_3V3 -> /Power/3V3_GROUP1
- U1 pad L12: /STM32/STM_CH3 -> /Connectors/STM_ESC.CH3
- U1 pad L13: /STM32/STM_CH4 -> /Connectors/STM_ESC.CH4
- U1 pad M1: Net-(F1-Pad1) -> GND
- U1 pad M11: /STM32/STM_CH7 -> /Connectors/STM_ESC.CH7
- U1 pad M13: /STM32/STM_CH8 -> /Connectors/STM_ESC.CH8
- U1 pad M14: /STM32/STM_CH6 -> /Connectors/STM_ESC.CH6
- U1 pad M15: /STM32/STM_CH5 -> /Connectors/STM_ESC.CH5
- U1 pad M6: /STM32/STM_SPI3_MOSI -> /STM32/STM_SPI3.MOSI
- U1 pad N1: STM_VREFM -> GND
- U1 pad N10: STM_3V3 -> /Power/3V3_GROUP1
- U1 pad N5: STM_SCALED_VDD_3V3_SENSORS -> /STM32/STM_SCALED_VDD_3V3_SENSORS
- U1 pad N8: STM_3V3 -> /Power/3V3_GROUP1
- U1 pad N9: STM_3V3 -> /Power/3V3_GROUP1
- U1 pad P1: STM_VREFP -> /Power/3V3_GROUP1
- U1 pad P7: /STM32/STM_I2C4_SDA -> /STM32/STM_I2C4.SDA
- U1 pad R1: STM_VDDA -> /Power/3V3_GROUP1
- U1 pad R3: /STM32/STM_SPI1_MOSI -> /STM32/STM_SPI1.MOSI
- U1 pad R7: /STM32/STM_I2C4_SCL -> /STM32/STM_I2C4.SCL
- U10 pad 48: unconnected-(U10-Pad48) -> Net-(R14-Pad1)
- U10 pad 49: unconnected-(U10-Pad49) -> Net-(R42-Pad2)
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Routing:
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- added copper zone on B.Cu, net GND
- added copper zone on F.Cu, net GND
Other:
- board outline added: 40 x 55 mm
- copper layers 2 -> 4

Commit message: продам гараж
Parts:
- C3, C36, C37, C5: moved to F.Cu
- moved C37 57.4 mm to (235.6, 115.6), turned to 0 degrees
- moved C36 51.7 mm to (232.2, 113.5), turned to 0 degrees
- moved LASER1 35.3 mm to (244.5, 113.8), turned to -90 degrees
- moved I2C1 35.3 mm to (210.4, 123.2), turned to 90 degrees
- moved C4 29.3 mm to (223.4, 121.8), turned to -90 degrees
- moved C5 9.00 mm to (198.0, 111.0), turned to 0 degrees
- moved C2 2.56 mm to (224.2, 119.0), turned to 45 degrees
- moved R41 0.57 mm to (223.5, 107.8), turned to 90 degrees
- moved R22 0.55 mm to (219.2, 108.2)
- moved R13 0.50 mm to (218.3, 108.2)
- moved R39 0.46 mm to (238.2, 128.7)
- moved C3 0.42 mm to (198.1, 109.9), turned to 0 degrees
- moved R55 0.35 mm to (238.2, 129.7)
- moved C28 0.20 mm to (239.7, 117.1)
- moved C26 0.15 mm to (238.1, 118.0)
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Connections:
- CAM0 pad MP: (no net) -> GND
- GPS1 pad MP: (no net) -> GND
- I2C1 pad MP: (no net) -> GND
- LASER1 pad MP: (no net) -> GND
- POWER1 pad MP: (no net) -> GND
- RC1 pad MP: (no net) -> GND
- TELEM1 pad MP: (no net) -> GND
- TELEM2 pad MP: (no net) -> GND
- U10 pad 15: unconnected-(U10-Pad15) -> /ESP32/ESP_UART1.RX
- U10 pad 16: unconnected-(U10-Pad16) -> /ESP32/ESP_UART1.TX
- U10 pad 50: /ESP32/ESP_UART1.RX -> unconnected-(U10-Pad50)
- U10 pad 55: /ESP32/ESP_UART1.TX -> unconnected-(U10-Pad55)
- U16 pad 9: GND -> (no net)
- Y4 pad 4: (no net) -> GND
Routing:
- net /Connectors/RPI_OUT_3V3: track 4.94 -> 86.4 mm, vias 0 -> 6
- net /STM32/SENSORS_3V3: track 12.5 -> 75.8 mm, vias 3 -> 11
- net /ESP32/ESP_UART1.TX: track 0.00 -> 43.5 mm, vias 0 -> 1
- net /ESP32/ESP_UART1.RX: track 0.00 -> 41.3 mm, vias 0 -> 1
- net /Connectors/STM_UART7.TX: track 0.00 -> 33.3 mm, vias 0 -> 2
- net /Connectors/STM_UART7.RX: track 0.00 -> 27.5 mm, vias 0 -> 4
- net /Connectors/STM_UART5.RX: track 0.00 -> 17.2 mm, vias 0 -> 3
- net VCC: track 123.0 -> 138.4 mm, vias 14 -> 15
- net /Connectors/STM_UART5.TX: track 0.00 -> 15.4 mm, vias 0 -> 1
- net /Connectors/RPI_LASER_I2C.SCL: track 0.00 -> 15.3 mm, vias 0 -> 2
- net /Connectors/RPI_LASER_I2C.SDA: track 0.00 -> 15.0 mm, vias 0 -> 2
- net /Connectors/STM_I2C1.SDA: track 36.5 -> 23.6 mm
- net /STM32/STM_VDD_3V3_SENSORS_EN: track 9.24 -> 16.3 mm, vias 0 -> 2
- net /Power/3V3_GROUP1: track 116.9 -> 121.3 mm, vias 18 -> 20
- net /Connectors/STM_I2C1.SCL: track 0.00 -> 2.05 mm, vias 0 -> 2
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
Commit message: )
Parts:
- moved LED1 13.0 mm to (263.5, 88.1)
- moved C2 0.74 mm to (223.7, 119.6), turned to 180 degrees
- moved C37 0.46 mm to (236.0, 115.7)
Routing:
- net /Power/3V3_GROUP1: track 121.3 -> 124.3 mm
- net /Connectors/PWR_IN_JST: track 5.13 -> 2.63 mm
- net GND: track 26.0 -> 27.9 mm

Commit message: autoroute test
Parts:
- moved LED1 16.2 mm to (254.6, 101.6)
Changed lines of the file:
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@@
   )
   (footprint "Connector_PinHeader_2.54mm:PinHeader_1x03_P2.54mm_Vertical" (layer "F.Cu")
-    (at 263.5 88.075)
+    (at 254.6 101.625)
     (descr "Through hole straight pin header, 1x03, 2.54mm pitch, single row")
     (tags "Through hole pin header THT 1x03 2.54mm single row")
